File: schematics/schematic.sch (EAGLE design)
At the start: 51 parts, among them IC1 74HC365, T1 BC547, X5 PN61729-S

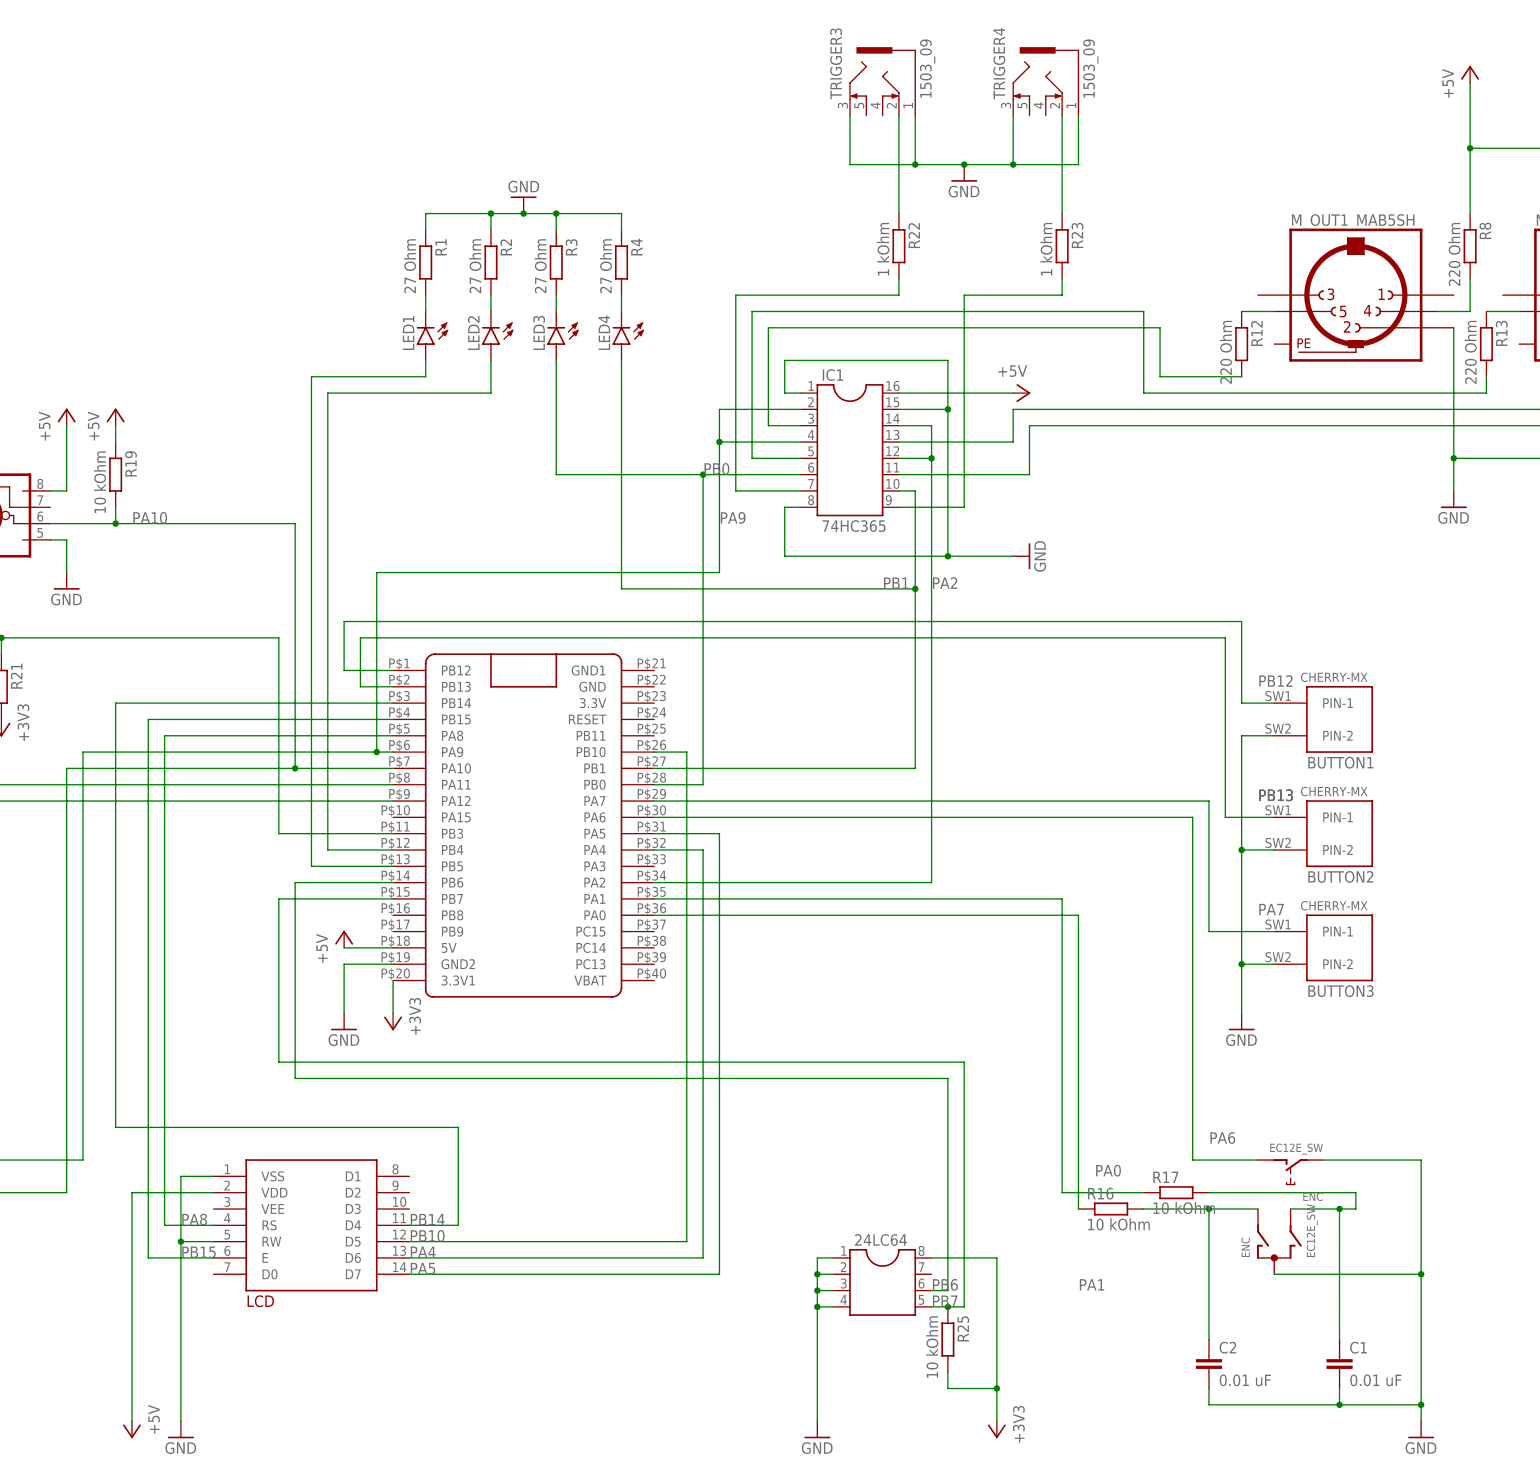
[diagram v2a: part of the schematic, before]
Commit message: updated timings
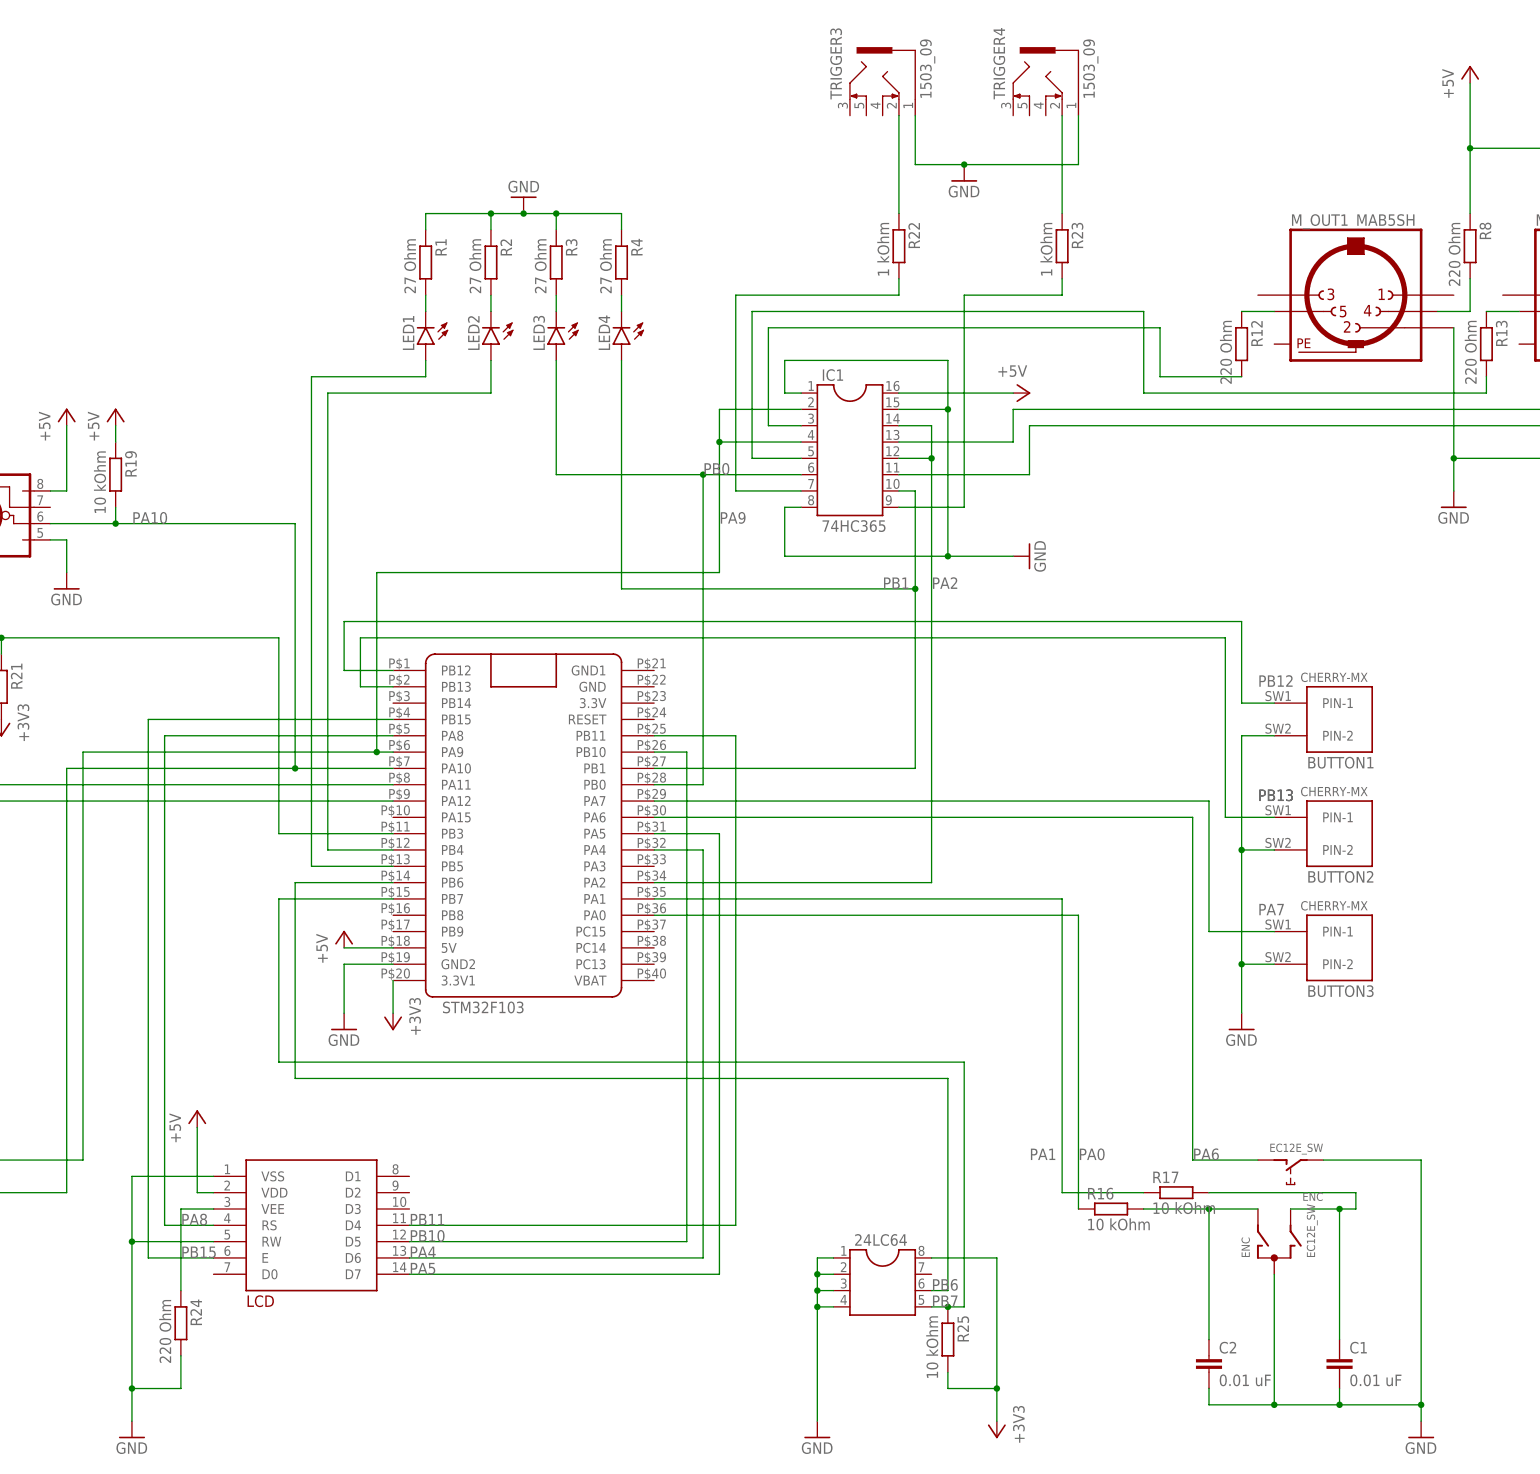
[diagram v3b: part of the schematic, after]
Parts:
- added R24: 220 Ohm, rcl:R-EU_0207/10
- renumbered U$1 to STM32F103
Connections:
- removed net PB14: LCD.D4, STM32F103.PB14
- new net N$27: LCD.VEE, R24.1
- new net PB11: LCD.D4, STM32F103.PB11
- net GND: now also R24.2; no longer TRIGGER3.3, TRIGGER4.3
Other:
- note added: "STM32F103"

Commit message: updated schematic
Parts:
- added R26: 10 kOhm, rcl:R-EU_0207/10
- added R27, R28: 100 Ohm, rcl:R-EU_0207/10
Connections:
- removed net N$23: C1.1, ENCG$1.B, R17.2
- new net N$22: ENCG$1.B, R28.1
- net +3V3: now also R16.2, R17.1, R26.2
- net GND: now also 24LC64.7
- net N$21: now also R27.2; no longer C2.1, R16.2
- net PA0: now also C2.1, R17.2, R27.1; no longer R16.1
- net PA1: now also C1.1, R16.1, R28.2; no longer R17.1
- net PB6: now also R26.1
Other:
- moved on the sheet: 24LC64, C1, C2, ENC, R16, R17, R25

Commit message: added footprints, started brd
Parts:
- M_IN, M_OUT1, M_OUT2, M_OUT3, M_OUT4: value MAB5SH -> DIN5PIN; device con-hirschmann:MAB5SH -> DIN_5pin:DIN5PIN
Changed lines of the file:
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@@
 <part name="GND4" library="supply1" library_urn="urn:adsk.eagle:library:371" deviceset="GND" device=""/>
 <part name="+3V2" library="supply1" library_urn="urn:adsk.eagle:library:371" deviceset="+3V3" device=""/>
-<part name="M_OUT1" library="con-hirschmann" library_urn="urn:adsk.eagle:library:153" deviceset="MAB5SH" device="" package3d_urn="urn:adsk.eagle:package:7443/1"/>
-<part name="M_OUT2" library="con-hirschmann" library_urn="urn:adsk.eagle:library:153" deviceset="MAB5SH" device="" package3d_urn="urn:adsk.eagle:package:7443/1"/>
-<part name="M_OUT3" library="con-hirschmann" library_urn="urn:adsk.eagle:library:153" deviceset="MAB5SH" device="" package3d_urn="urn:adsk.eagle:package:7443/1"/>
-<part name="M_OUT4" library="con-hirschmann" library_urn="urn:adsk.eagle:library:153" deviceset="MAB5SH" device="" package3d_urn="urn:adsk.eagle:package:7443/1"/>
+<part name="M_OUT1" library="DIN_5pin" deviceset="DIN5PIN" device=""/>
+<part name="M_OUT2" library="DIN_5pin" deviceset="DIN5PIN" device=""/>
+<part name="M_OUT3" library="DIN_5pin" deviceset="DIN5PIN" device=""/>
+<part name="M_OUT4" library="DIN_5pin" deviceset="DIN5PIN" device=""/>
 <part name="X5" library="con-berg" library_urn="urn:adsk.eagle:library:130" deviceset="PN61729-S" device="" package3d_urn="urn:adsk.eagle:package:6149/1"/>
 <part name="P+3" library="supply1" library_urn="urn:adsk.eagle:library:371" deviceset="+5V" device=""/>
@@
 <part name="C1" library="rcl" library_urn="urn:adsk.eagle:library:334" deviceset="C-EU" device="050-025X075" package3d_urn="urn:adsk.eagle:package:23637/1" value="0.01 uF"/>
 <part name="C2" library="rcl" library_urn="urn:adsk.eagle:library:334" deviceset="C-EU" device="050-025X075" package3d_urn="urn:adsk.eagle:package:23637/1" value="0.01 uF"/>
-<part name="M_IN" library="con-hirschmann" library_urn="urn:adsk.eagle:library:153" deviceset="MAB5SH" device="" package3d_urn="urn:adsk.eagle:package:7443/1"/>
+<part name="M_IN" library="DIN_5pin" deviceset="DIN5PIN" device=""/>
 <part name="OK1" library="optocoupler" library_urn="urn:adsk.eagle:library:320" deviceset="6N137" device="" package3d_urn="urn:adsk.eagle:package:21941/1"/>
 <part name="D1" library="diode" library_urn="urn:adsk.eagle:library:210" deviceset="1N4446" device="" package3d_urn="urn:adsk.eagle:package:43344/2"/>

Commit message: finished first version of schematic;
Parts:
- added C3, C5: 0.1 uF, rcl:C-EU050-025X075
- added C4: 10uF, rcl:CPOL-EUE2.5-6
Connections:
- net +3V3: now also C5.2
- net +5V: now also C3.1, C4.+
- net GND: now also C3.2, C4.-, C5.1, STM32F103.GND, STM32F103.GND1
- net PA4: now also LCD.D4; no longer LCD.D6
- net PA5: now also LCD.D5; no longer LCD.D7
- net PB10: now also LCD.D6; no longer LCD.D5
- net PB11: now also LCD.D7; no longer LCD.D4

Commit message: fixed some schematic errors
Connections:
- net GND: no longer X5.S1, X5.S2
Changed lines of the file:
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@@
 <pinref part="GND5" gate="1" pin="GND"/>
 <wire x1="-78.74" y1="30.48" x2="-78.74" y2="15.24" width="0.1524" layer="91"/>
-<wire x1="-78.74" y1="30.48" x2="-73.66" y2="30.48" width="0.1524" layer="91"/>
-<junction x="-78.74" y="30.48"/>
-<pinref part="X5" gate="G$1" pin="S1"/>
-<wire x1="-73.66" y1="30.48" x2="-73.66" y2="33.02" width="0.1524" layer="91"/>
-<wire x1="-73.66" y1="30.48" x2="-71.12" y2="30.48" width="0.1524" layer="91"/>
-<junction x="-73.66" y="30.48"/>
-<pinref part="X5" gate="G$1" pin="S2"/>
-<wire x1="-71.12" y1="30.48" x2="-71.12" y2="33.02" width="0.1524" layer="91"/>
 </segment>
 <segment>
